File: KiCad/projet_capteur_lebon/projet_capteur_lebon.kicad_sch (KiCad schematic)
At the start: 4 parts, among them J1 Power, J2 Digital/PWM, J3 Analog, J4 Digital/PWM

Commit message: Création symbole + empreinte OLED
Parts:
- added U1: ~, librairie_empreintes:SIP-4, symbol librairie symboles:OLED
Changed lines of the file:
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@@
+		)
+	)
+	(symbol
+		(lib_id "librairie symboles:OLED")
+		(at 114.3 48.26 0)
+		(unit 1)
+		(exclude_from_sim no)
+		(in_bom yes)
+		(on_board yes)
+		(dnp no)
+		(fields_autoplaced yes)
+		(property "Reference" "U1"
+			(at 130.81 46.3549 0)
+			(effects
+				(font
+					(size 1.27 1.27)
+				)
+				(justify left)
+			)
+		)
+		(property "Value" "~"
+			(at 130.81 48.26 0)
+			(effects
+				(font
+					(size 1.27 1.27)
+				)
+				(justify left)
+			)
+		)
+		(property "Footprint" "librairie_empreintes:SIP-4"
+			(at 114.3 48.26 0)
+			(effects
+				(font
+					(size 1.27 1.27)
+				)
+				(hide yes)
+			)
+		)
+		(property "Datasheet" ""
+			(at 114.3 48.26 0)
+			(effects
+				(font
+					(size 1.27 1.27)
+				)
+				(hide yes)
+			)
+		)
+		(property "Description" ""
+			(at 114.3 48.26 0)
+			(effects
+				(font
+					(size 1.27 1.27)
+				)
+				(hide yes)
+			)
+		)
+		(pin "2"
+		)
+		(pin "3"
+		)
+		(pin "4"
+		)
+		(pin "1"
+		)
+		(instances
+			(project ""
+				(path "/e63e39d7-6ac0-4ffd-8aa3-1841a4541b55"
+					(reference "U1")
+					(unit 1)
+				)
+			)
 		)
 	)

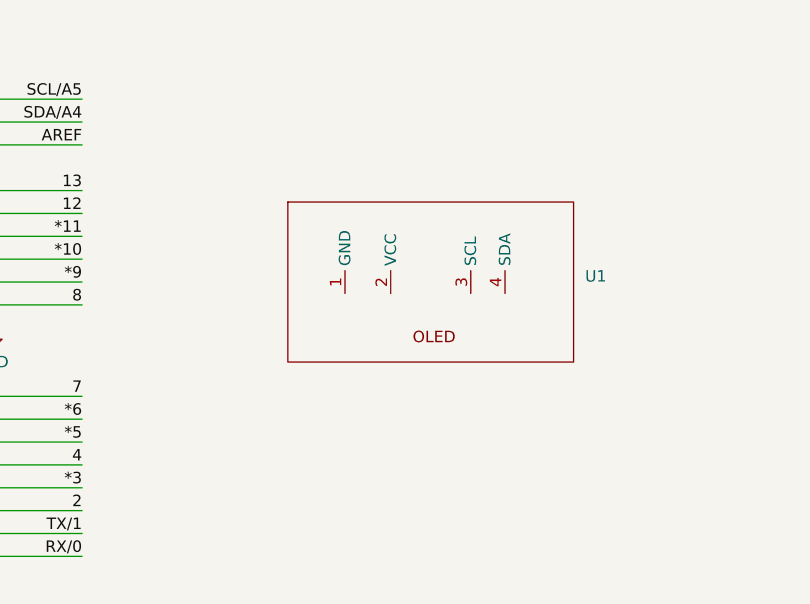
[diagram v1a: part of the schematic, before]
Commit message: modèle 3d oled + flex sensor
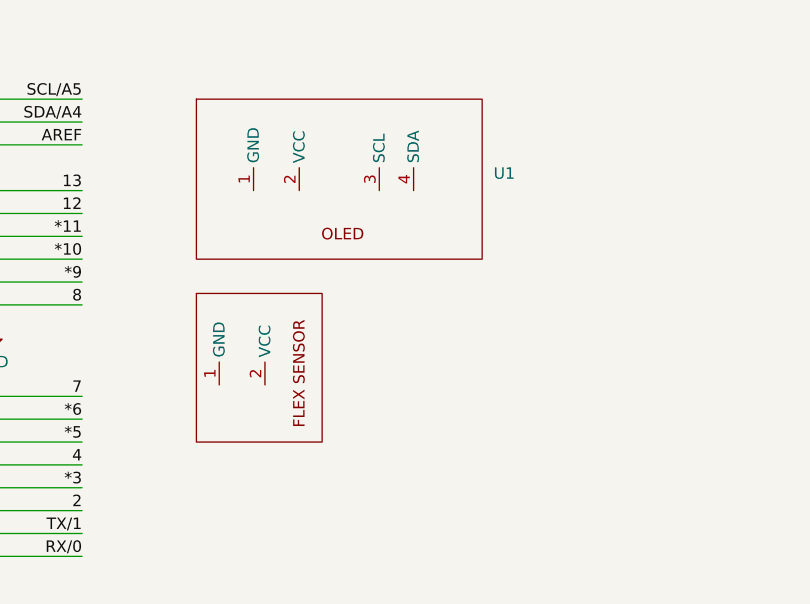
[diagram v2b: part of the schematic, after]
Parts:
- added U2: ~, librairie_empreintes:SIP-2, symbol librairie symboles:FLEX_SENSOR
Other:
- moved on the sheet: U1
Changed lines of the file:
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@@
+	)
+	(symbol
+		(lib_id "librairie symboles:FLEX_SENSOR")
+		(at 93.98 58.42 0)
+		(unit 1)
+		(exclude_from_sim no)
+		(in_bom yes)
+		(on_board yes)
+		(dnp no)
+		(fields_autoplaced yes)
+		(property "Reference" "U2"
+			(at 93.98 58.42 0)
+			(effects
+				(font
+					(size 1.27 1.27)
+				)
+				(hide yes)
+			)
+		)
+		(property "Value" "~"
+			(at 102.87 56.515 0)
+			(effects
+				(font
+					(size 1.27 1.27)
+				)
+				(justify left)
+			)
+		)
+		(property "Footprint" "librairie_empreintes:SIP-2"
+			(at 93.98 58.42 0)
+			(effects
+				(font
+					(size 1.27 1.27)
+				)
+				(hide yes)
+			)
+		)
+		(property "Datasheet" ""
+			(at 93.98 58.42 0)
+			(effects
+				(font
+					(size 1.27 1.27)
+				)
+				(hide yes)
+			)
+		)
+		(property "Description" ""
+			(at 93.98 58.42 0)
+			(effects
+				(font
+					(size 1.27 1.27)
+				)
+				(hide yes)
+			)
+		)
+		(pin "1"
+		)
+		(pin "2"
+		)
+		(instances
+			(project ""
+				(path "/e63e39d7-6ac0-4ffd-8aa3-1841a4541b55"
+					(reference "U2")
+					(unit 1)
+				)
+			)
+		)
 	)
 	(symbol
@@
 	(symbol
 		(lib_id "librairie symboles:OLED")
-		(at 114.3 48.26 0)
+		(at 104.14 36.83 0)
 		(unit 1)
 		(exclude_from_sim no)
@@
 		(fields_autoplaced yes)
 		(property "Reference" "U1"
-			(at 130.81 46.3549 0)
+			(at 120.65 34.9249 0)
 			(effects
 				(font
@@
 		)
 		(property "Value" "~"
-			(at 130.81 48.26 0)
+			(at 120.65 36.83 0)
 			(effects
 				(font
@@
 		)
 		(property "Footprint" "librairie_empreintes:SIP-4"
-			(at 114.3 48.26 0)
+			(at 104.14 36.83 0)
 			(effects
 				(font
@@
 		)
 		(property "Datasheet" ""
-			(at 114.3 48.26 0)
+			(at 104.14 36.83 0)
 			(effects
 				(font
@@
 		)
 		(property "Description" ""
-			(at 114.3 48.26 0)
+			(at 104.14 36.83 0)
 			(effects
 				(font

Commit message: creation ampli
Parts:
- added C1, C2: 100n, symbol Device:C
- added C4: 1u, symbol Device:C
- added R1, R3: 100k, symbol Device:R
- added R5: 10k, symbol Device:R
- added R6: 1k, symbol Device:R
- added U4: ~, librairie_empreintes:DIP-8_296, symbol librairie symboles:AO_LTC1050
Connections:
- net +5V: now also U4.7 (VCC+)
- net GND: now also C1.2, C2.2, R1.2, U4.4 (VCC-)
- new net: C1.1, R1.1, R5.2, U4.3 (IN+)
- new net: C4.1, R3.1, U4.2 (IN-)
- new net: C4.2, R3.2, R6.1, U4.6 (OUT)
- new net output: C2.1, R6.2

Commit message: travail sur l'ampli transimpedance
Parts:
- C1, C2, C4: footprint (none) -> librairie_empreintes:C_Disc_D6.0mm_W2.5mm_P5.00mm
- R1, R3, R5, R6: footprint (none) -> librairie_empreintes:R_Axial_DIN0207_L6.3mm_D2.5mm_P5.08mm_Vertical
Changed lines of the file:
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@@
 			)
 		)
-		(property "Footprint" ""
+		(property "Footprint" "librairie_empreintes:C_Disc_D6.0mm_W2.5mm_P5.00mm"
 			(at 169.8752 107.95 0)
 			(effects
@@
 			)
 		)
-		(property "Footprint" ""
+		(property "Footprint" "librairie_empreintes:C_Disc_D6.0mm_W2.5mm_P5.00mm"
 			(at 61.9252 110.49 0)
 			(effects
@@
 			)
 		)
-		(property "Footprint" ""
+		(property "Footprint" "librairie_empreintes:R_Axial_DIN0207_L6.3mm_D2.5mm_P5.08mm_Vertical"
 			(at 74.422 106.68 90)
 			(effects
@@
 			)
 		)
-		(property "Footprint" ""
+		(property "Footprint" "librairie_empreintes:C_Disc_D6.0mm_W2.5mm_P5.00mm"
 			(at 138.1252 92.71 0)
 			(effects
@@
 			)
 		)
-		(property "Footprint" ""
+		(property "Footprint" "librairie_empreintes:R_Axial_DIN0207_L6.3mm_D2.5mm_P5.08mm_Vertical"
 			(at 158.75 99.568 90)
 			(effects
@@
 			)
 		)
-		(property "Footprint" ""
+		(property "Footprint" "librairie_empreintes:R_Axial_DIN0207_L6.3mm_D2.5mm_P5.08mm_Vertical"
 			(at 145.542 88.9 90)
 			(effects
@@
 			)
 		)
-		(property "Footprint" ""
+		(property "Footprint" "librairie_empreintes:R_Axial_DIN0207_L6.3mm_D2.5mm_P5.08mm_Vertical"
 			(at 48.26 100.838 90)
 			(effects

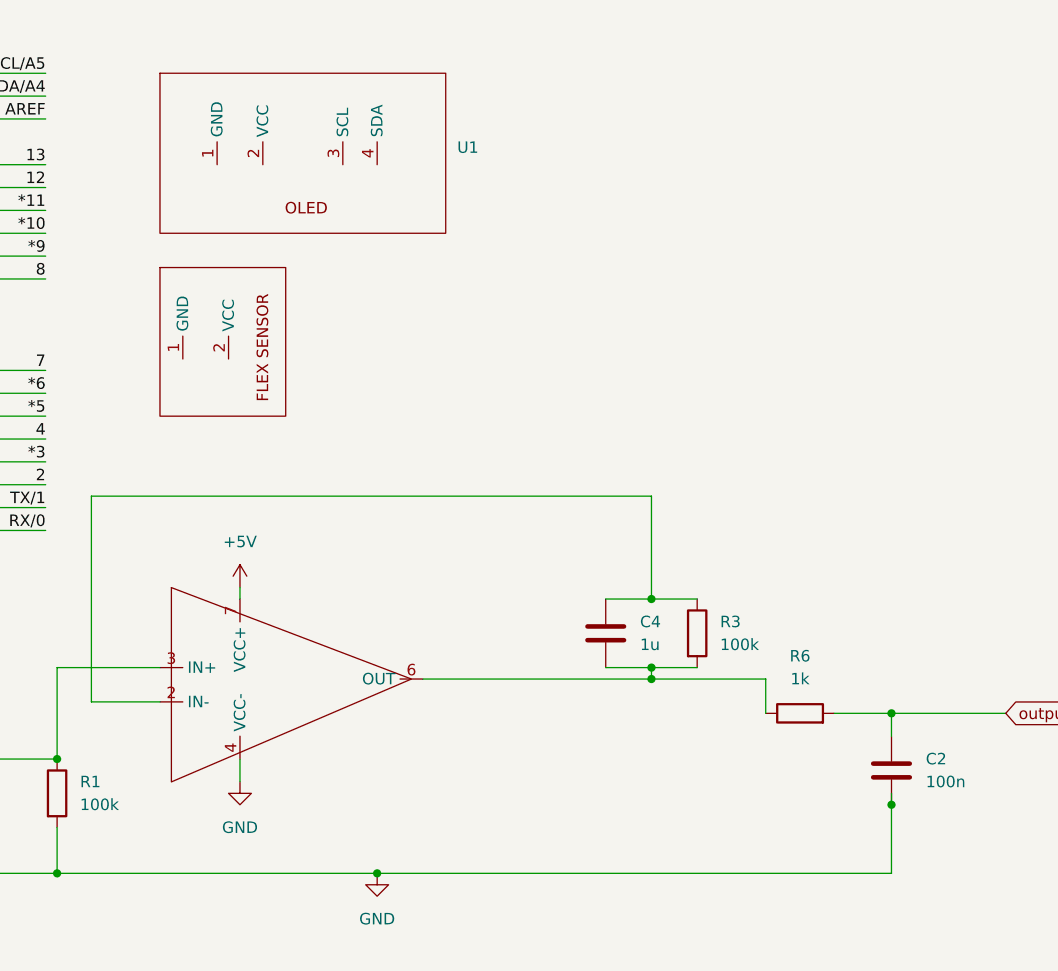
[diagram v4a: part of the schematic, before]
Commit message: mep bluetooth et fin ampli
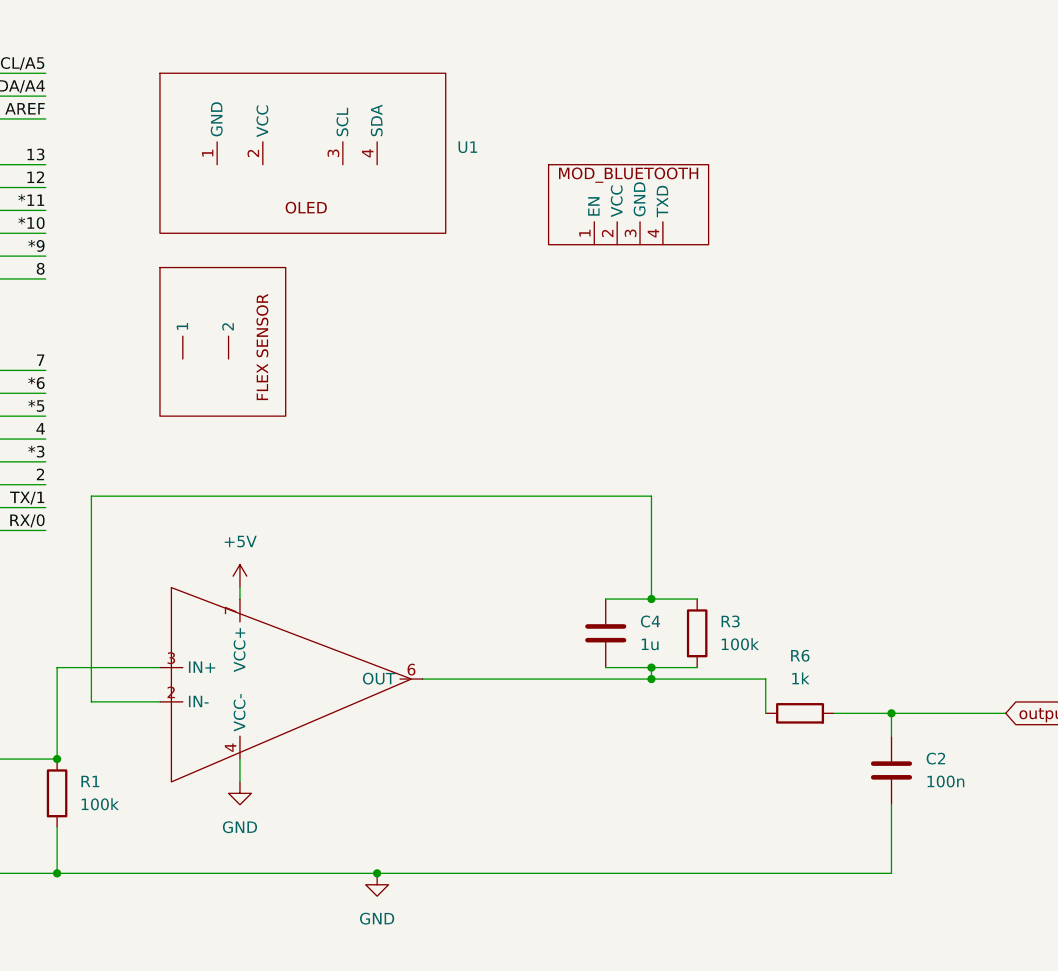
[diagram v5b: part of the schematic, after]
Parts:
- removed U2: ~, librairie_empreintes:SIP-2, symbol librairie symboles:FLEX_SENSOR
- added U3: ~, librairie_empreintes:SIP-2, symbol librairie symboles:MOD_BLUETOOTH
- added U5: ~, librairie_empreintes:BLUETOOTH, symbol librairie symboles:FLEX_SENSOR
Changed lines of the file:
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@@
-	)
-	(junction
-		(at 168.91 107.95)
-		(diameter 0)
-		(color 0 0 0 0)
 	)
 	(junction
@@
 	(wire
 		(pts
+			(xy 168.91 107.95) (xy 168.91 115.57)
+		)
+		(stroke
+			(width 0)
+			(type default)
+		)
+	)
+	(wire
+		(pts
 			(xy 31.75 44.45) (xy 31.75 46.99)
 		)
@@
 	(wire
 		(pts
-			(xy 168.91 107.95) (xy 168.91 115.57)
-		)
-		(stroke
-			(width 0)
-			(type default)
-		)
-	)
-	(wire
-		(pts
 			(xy 34.29 46.99) (xy 31.75 46.99)
 		)
@@
 			(width 0)
 			(type solid)
-		)
-	)
-	(wire
-		(pts
-			(xy 168.91 106.68) (xy 168.91 107.95)
-		)
-		(stroke
-			(width 0)
-			(type default)
 		)
 	)
@@
 	)
 	(symbol
+		(lib_id "librairie symboles:MOD_BLUETOOTH")
+		(at 138.43 45.72 0)
+		(unit 1)
+		(exclude_from_sim no)
+		(in_bom yes)
+		(on_board yes)
+		(dnp no)
+		(fields_autoplaced yes)
+		(property "Reference" "U3"
+			(at 138.43 45.72 0)
+			(effects
+				(font
+					(size 1.27 1.27)
+				)
+				(hide yes)
+			)
+		)
+		(property "Value" "~"
+			(at 149.86 41.2722 0)
+			(effects
+				(font
+					(size 1.27 1.27)
+				)
+				(justify left)
+			)
+		)
+		(property "Footprint" "librairie_empreintes:SIP-2"
+			(at 138.43 45.72 0)
+			(effects
+				(font
+					(size 1.27 1.27)
+				)
+				(hide yes)
+			)
+		)
+		(property "Datasheet" ""
+			(at 138.43 45.72 0)
+			(effects
+				(font
+					(size 1.27 1.27)
+				)
+				(hide yes)
+			)
+		)
+		(property "Description" ""
+			(at 138.43 45.72 0)
+			(effects
+				(font
+					(size 1.27 1.27)
+				)
+				(hide yes)
+			)
+		)
+		(pin "1"
+		)
+		(pin "2"
+		)
+		(pin "3"
+		)
+		(pin "4"
+		)
+		(instances
+			(project ""
+				(path "/e63e39d7-6ac0-4ffd-8aa3-1841a4541b55"
+					(reference "U3")
+					(unit 1)
+				)
+			)
+		)
+	)
+	(symbol
 		(lib_id "power:GND")
 		(at 111.76 115.57 0)
@@
 	)
 	(symbol
+		(lib_name "FLEX_SENSOR_1")
 		(lib_id "librairie symboles:FLEX_SENSOR")
 		(at 93.98 58.42 0)
@@
 		(dnp no)
 		(fields_autoplaced yes)
-		(property "Reference" "U2"
+		(property "Reference" "U5"
 			(at 93.98 58.42 0)
 			(effects
@@
 			)
 		)
-		(property "Footprint" "librairie_empreintes:SIP-2"
+		(property "Footprint" "librairie_empreintes:BLUETOOTH"
 			(at 93.98 58.42 0)
 			(effects
@@
 			)
 		)
-		(pin "1"
-		)
-		(pin "2"
+		(pin ""
+		)
+		(pin ""
 		)
 		(instances
 			(project ""
 				(path "/e63e39d7-6ac0-4ffd-8aa3-1841a4541b55"
-					(reference "U2")
+					(reference "U5")
 					(unit 1)
 				)

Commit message: resistance flex
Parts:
- added R2: 47k, librairie_empreintes:R_Axial_DIN0207_L6.3mm_D2.5mm_P5.08mm_Vertical, symbol Device:R
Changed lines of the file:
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@@
+	)
+	(symbol
+		(lib_id "Device:R")
+		(at 111.76 55.88 0)
+		(unit 1)
+		(exclude_from_sim no)
+		(in_bom yes)
+		(on_board yes)
+		(dnp no)
+		(fields_autoplaced yes)
+		(property "Reference" "R2"
+			(at 114.3 54.6099 0)
+			(effects
+				(font
+					(size 1.27 1.27)
+				)
+				(justify left)
+			)
+		)
+		(property "Value" "47k"
+			(at 114.3 57.1499 0)
+			(effects
+				(font
+					(size 1.27 1.27)
+				)
+				(justify left)
+			)
+		)
+		(property "Footprint" "librairie_empreintes:R_Axial_DIN0207_L6.3mm_D2.5mm_P5.08mm_Vertical"
+			(at 109.982 55.88 90)
+			(effects
+				(font
+					(size 1.27 1.27)
+				)
+				(hide yes)
+			)
+		)
+		(property "Datasheet" "~"
+			(at 111.76 55.88 0)
+			(effects
+				(font
+					(size 1.27 1.27)
+				)
+				(hide yes)
+			)
+		)
+		(property "Description" "Resistor"
+			(at 111.76 55.88 0)
+			(effects
+				(font
+					(size 1.27 1.27)
+				)
+				(hide yes)
+			)
+		)
+		(pin "1"
+		)
+		(pin "2"
+		)
+		(instances
+			(project "projet_capteur_lebon"
+				(path "/e63e39d7-6ac0-4ffd-8aa3-1841a4541b55"
+					(reference "R2")
+					(unit 1)
+				)
+			)
+		)
 	)
 	(symbol

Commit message: encodeur rot + verifs
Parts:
- added U2: ~, librairie_empreintes:ENCODEUR ROT, symbol librairie symboles:ENCODEUR_ROTATOIRE
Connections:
- net +5V: now also U5. (2)
- net GND: now also R2.2, U1.1 (GND), U3.4 (TXD), U2.5 (GND)
- net Analog voltage: now reaches U5. (2)
- net Analog voltage: now also R2.1
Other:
- moved on the sheet: C1, C2, C4, R1, R2, R3, R5, R6

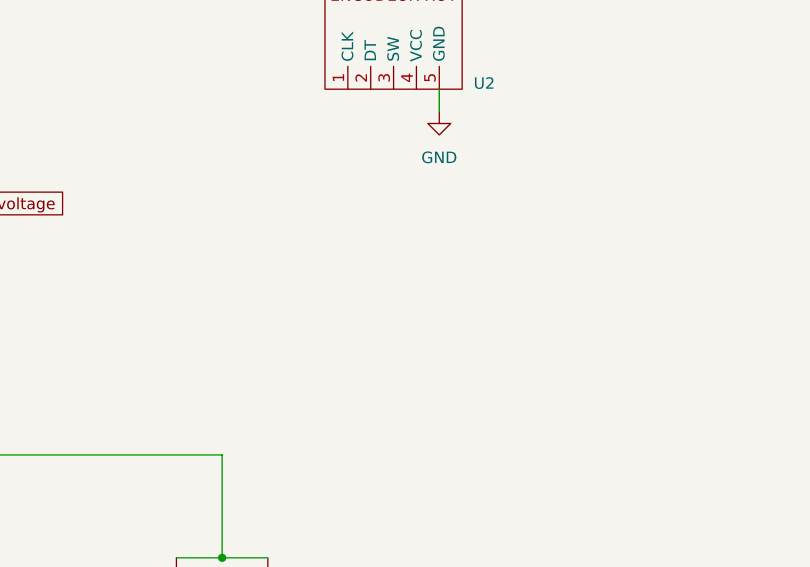
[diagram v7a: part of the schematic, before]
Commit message: capteur graphite symbole et empreintes
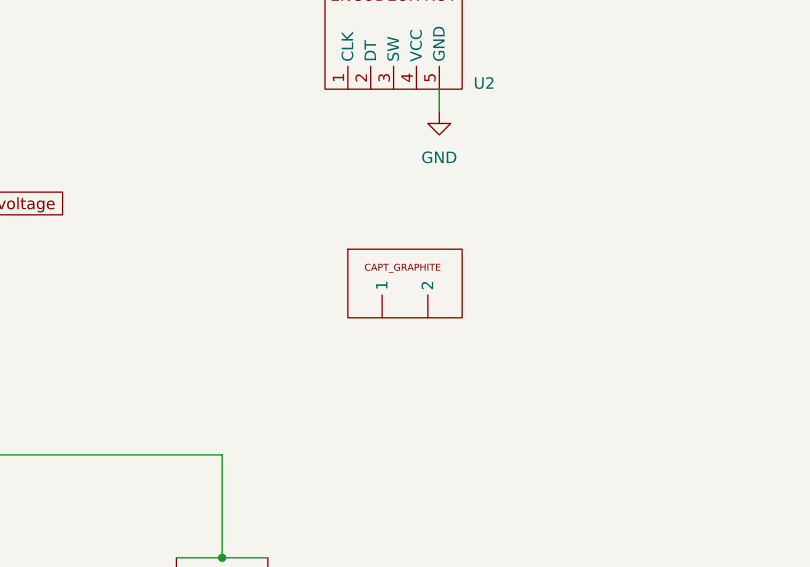
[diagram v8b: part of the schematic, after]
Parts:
- added U6: ~, librairie_empreintes:CAPTEUR_GRAPHITE, symbol librairie symboles:CAPTEUR_GRAPHITE
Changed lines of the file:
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@@
+	)
+	(symbol
+		(lib_id "librairie symboles:CAPTEUR_GRAPHITE")
+		(at 157.48 96.52 0)
+		(unit 1)
+		(exclude_from_sim no)
+		(in_bom yes)
+		(on_board yes)
+		(dnp no)
+		(fields_autoplaced yes)
+		(property "Reference" "U6"
+			(at 157.48 96.52 0)
+			(effects
+				(font
+					(size 1.27 1.27)
+				)
+				(hide yes)
+			)
+		)
+		(property "Value" "~"
+			(at 165.1 92.71 0)
+			(effects
+				(font
+					(size 1.27 1.27)
+				)
+				(justify left)
+			)
+		)
+		(property "Footprint" "librairie_empreintes:CAPTEUR_GRAPHITE"
+			(at 157.48 96.52 0)
+			(effects
+				(font
+					(size 1.27 1.27)
+				)
+				(hide yes)
+			)
+		)
+		(property "Datasheet" ""
+			(at 157.48 96.52 0)
+			(effects
+				(font
+					(size 1.27 1.27)
+				)
+				(hide yes)
+			)
+		)
+		(property "Description" ""
+			(at 157.48 96.52 0)
+			(effects
+				(font
+					(size 1.27 1.27)
+				)
+				(hide yes)
+			)
+		)
+		(pin ""
+		)
+		(pin ""
+		)
+		(instances
+			(project ""
+				(path "/e63e39d7-6ac0-4ffd-8aa3-1841a4541b55"
+					(reference "U6")
+					(unit 1)
+				)
+			)
+		)
 	)
 	(symbol
